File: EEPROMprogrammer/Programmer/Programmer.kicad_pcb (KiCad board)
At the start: 2 copper layers, 58.4 x 47 mm, 4 parts, among them U1 74HC595, U2 74HC595, U3 AT28C256B15PU

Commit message: In situ programming hw
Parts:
- removed U3: AT28C256B15PU, Package_DIP:DIP-28_W15.24mm
- added D1: LED, LED_THT:LED_D3.0mm, F.Cu at (132.1, 67.3)
- added J1: Conn_01x16_Female, Connector_PinSocket_2.54mm:PinSocket_1x16_P2.54mm_Vertical, F.Cu at (114.0, 83.8)
- added J2: Conn_01x06_Female, Connector_PinSocket_2.54mm:PinSocket_1x06_P2.54mm_Vertical, F.Cu at (132.1, 61.0)
- added J3: Conn_01x08_Female, Connector_PinSocket_2.54mm:PinSocket_1x08_P2.54mm_Vertical, F.Cu at (114.0, 78.7)
- added R1: 2k2, Resistor_THT:R_Axial_DIN0204_L3.6mm_D1.6mm_P7.62mm_Horizontal, F.Cu at (146.1, 68.6)
- added REF**: OSHW-Logo2_7.3x6mm_SilkScreen, Symbol:OSHW-Logo2_7.3x6mm_SilkScreen, F.Cu at (124.5, 73.0)
- moved A1 38.9 mm to (134.6, 76.2)
- moved U2 9.16 mm to (120.7, 104.1), turned to 0 degrees
- moved U1 7.94 mm to (120.7, 82.5), turned to 0 degrees
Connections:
- A1 pad 19: /~OE -> /~RE
- A1 pad 20: Net-(A1-Pad20) -> /~BUSRQ
- A1 pad 21: Net-(A1-Pad21) -> /~BUSACK
- A1 pad 22: Net-(A1-Pad22) -> /~AOE
- A1 pad 6: /SHIFTCLK -> /ADRCLK
- A1 pad 7: /ADRCLK -> /SHIFTCLK
- U1 pad 13: GND -> /~AOE
- U2 pad 13: GND -> /~AOE
- U2 pad 7: Net-(U2-Pad7) -> /A15
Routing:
- net +5V: track 0.00 -> 100.7 mm, vias 0 -> 1
- net /~RE: track 0.00 -> 70.1 mm, vias 0 -> 2
- net /~BUSRQ: track 0.00 -> 64.8 mm, vias 0 -> 2
- net /~AOE: track 0.00 -> 61.9 mm, vias 0 -> 1
- net /~OE: track 60.8 -> 0.00 mm, vias 1 -> 0
- net /~BUSACK: track 0.00 -> 60.6 mm
- net /A9: track 51.8 -> 7.69 mm, vias 1 -> 0
- net /A8: track 60.4 -> 16.3 mm, vias 1 -> 0
- net /A11: track 44.9 -> 7.66 mm, vias 1 -> 0
- net /A13: track 44.5 -> 7.66 mm, vias 1 -> 0
- net /A10: track 42.2 -> 7.69 mm, vias 1 -> 0
- net /A12: track 36.8 -> 7.66 mm
- net Net-(U1-Pad9): track 41.0 -> 12.0 mm
- net /A14: track 34.4 -> 7.66 mm
- net /D7: track 74.8 -> 49.2 mm, vias 0 -> 1
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- added copper zone on F.Cu, net GND
- removed copper zone on F.Cu, net +5V
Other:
- board size 58.4 x 47 mm -> 40 x 65 mm
- net class Default: via_dia 0.8 -> 0.6; via_drill 0.4 -> 0.3
- net class Power added: clearance 0.3, trace_width 0.5, via_dia 0.8, via_drill 0.4
- board text added: "+5V"
- board text added: "0"
- board text added: "15"
- board text added: "7"
- board text added: "A0"
- board text added: "A1"
- board text added: "A2"
- board text added: "A3"
- board text added: "ACLK"
- board text added: "Address"
- board text added: "BUSACK"
- board text added: "D13"
- board text added: "Data"
- board text added: "GND"
- board text added: "SCLK"
- board text added: "SERA"
- board text added: "~AOE"
- board text added: "~BUSACK"
- board text added: "~BUSRQ"
- board text added: "~RE"
- board text added: "~WE"

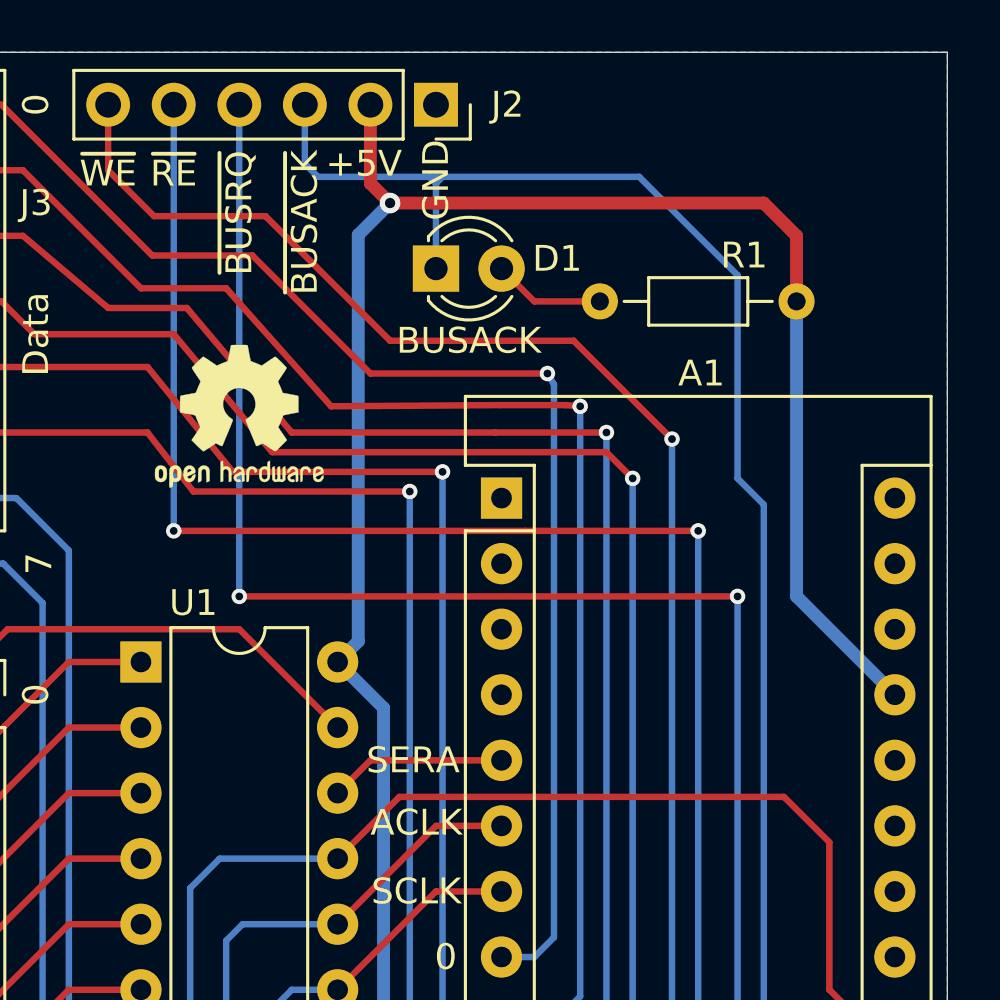
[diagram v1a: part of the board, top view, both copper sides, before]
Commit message: Pull up AOE
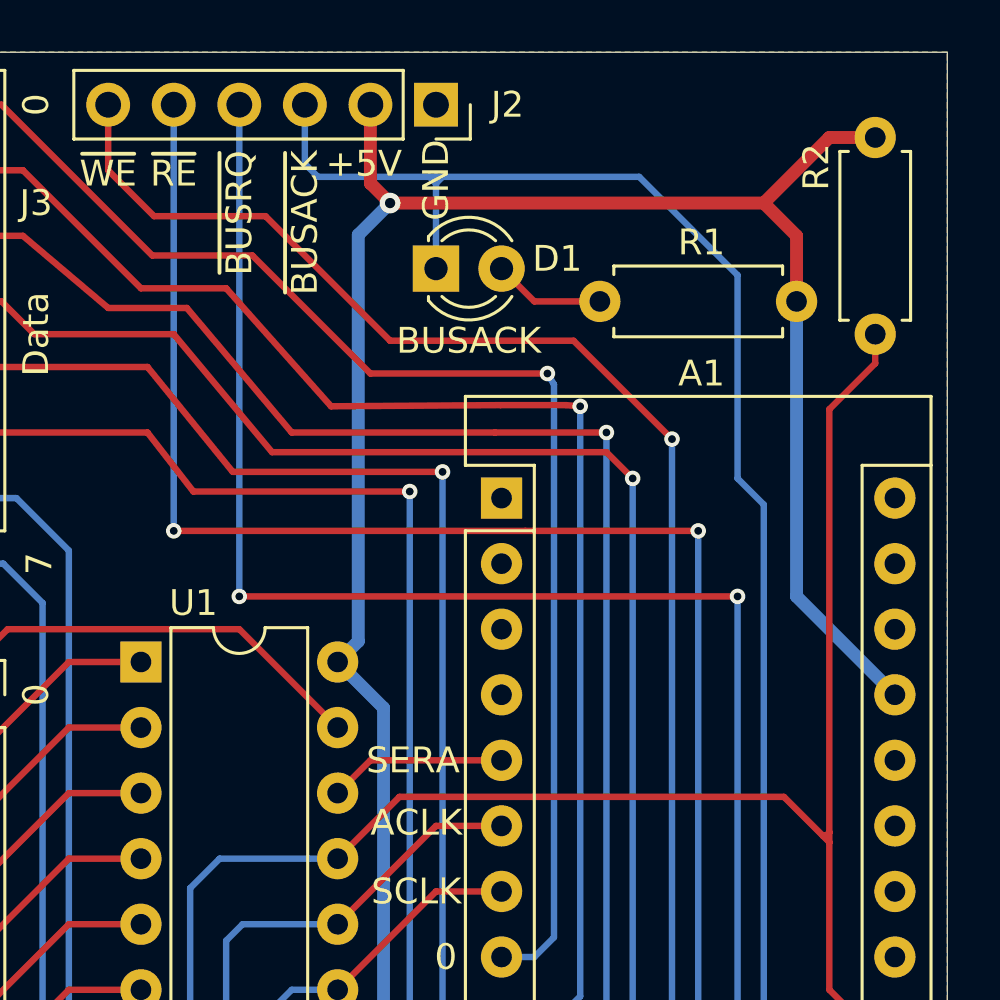
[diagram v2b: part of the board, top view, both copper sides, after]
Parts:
- removed REF**: OSHW-Logo2_7.3x6mm_SilkScreen, Symbol:OSHW-Logo2_7.3x6mm_SilkScreen
- added R2: 10k, Resistor_THT:R_Axial_DIN0207_L6.3mm_D2.5mm_P7.62mm_Horizontal, F.Cu at (149.1, 69.8)
- R1: footprint Resistor_THT:R_Axial_DIN0204_L3.6mm_D1.6mm_P7.62mm_Horizontal -> Resistor_THT:R_Axial_DIN0207_L6.3mm_D2.5mm_P7.62mm_Horizontal
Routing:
- net /~AOE: track 61.9 -> 82.6 mm
- net +5V: track 100.7 -> 106.1 mm
